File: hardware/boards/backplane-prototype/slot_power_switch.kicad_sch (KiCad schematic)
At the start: 14 parts, among them Q1 SQD50P06-15L_GE3, Q2 BSS123, U1 74HC595D,118

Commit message: chore: checkpoint current board layout
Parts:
- U1: value 74HC595D,118 -> 74HC595D
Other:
- title: Slot 1 High-Side Power Switch -> Backplane Prototype
- moved on the sheet: C1, D9, Q1, Q2, R15, R16, R17, R18, R19, R20, R21, R22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

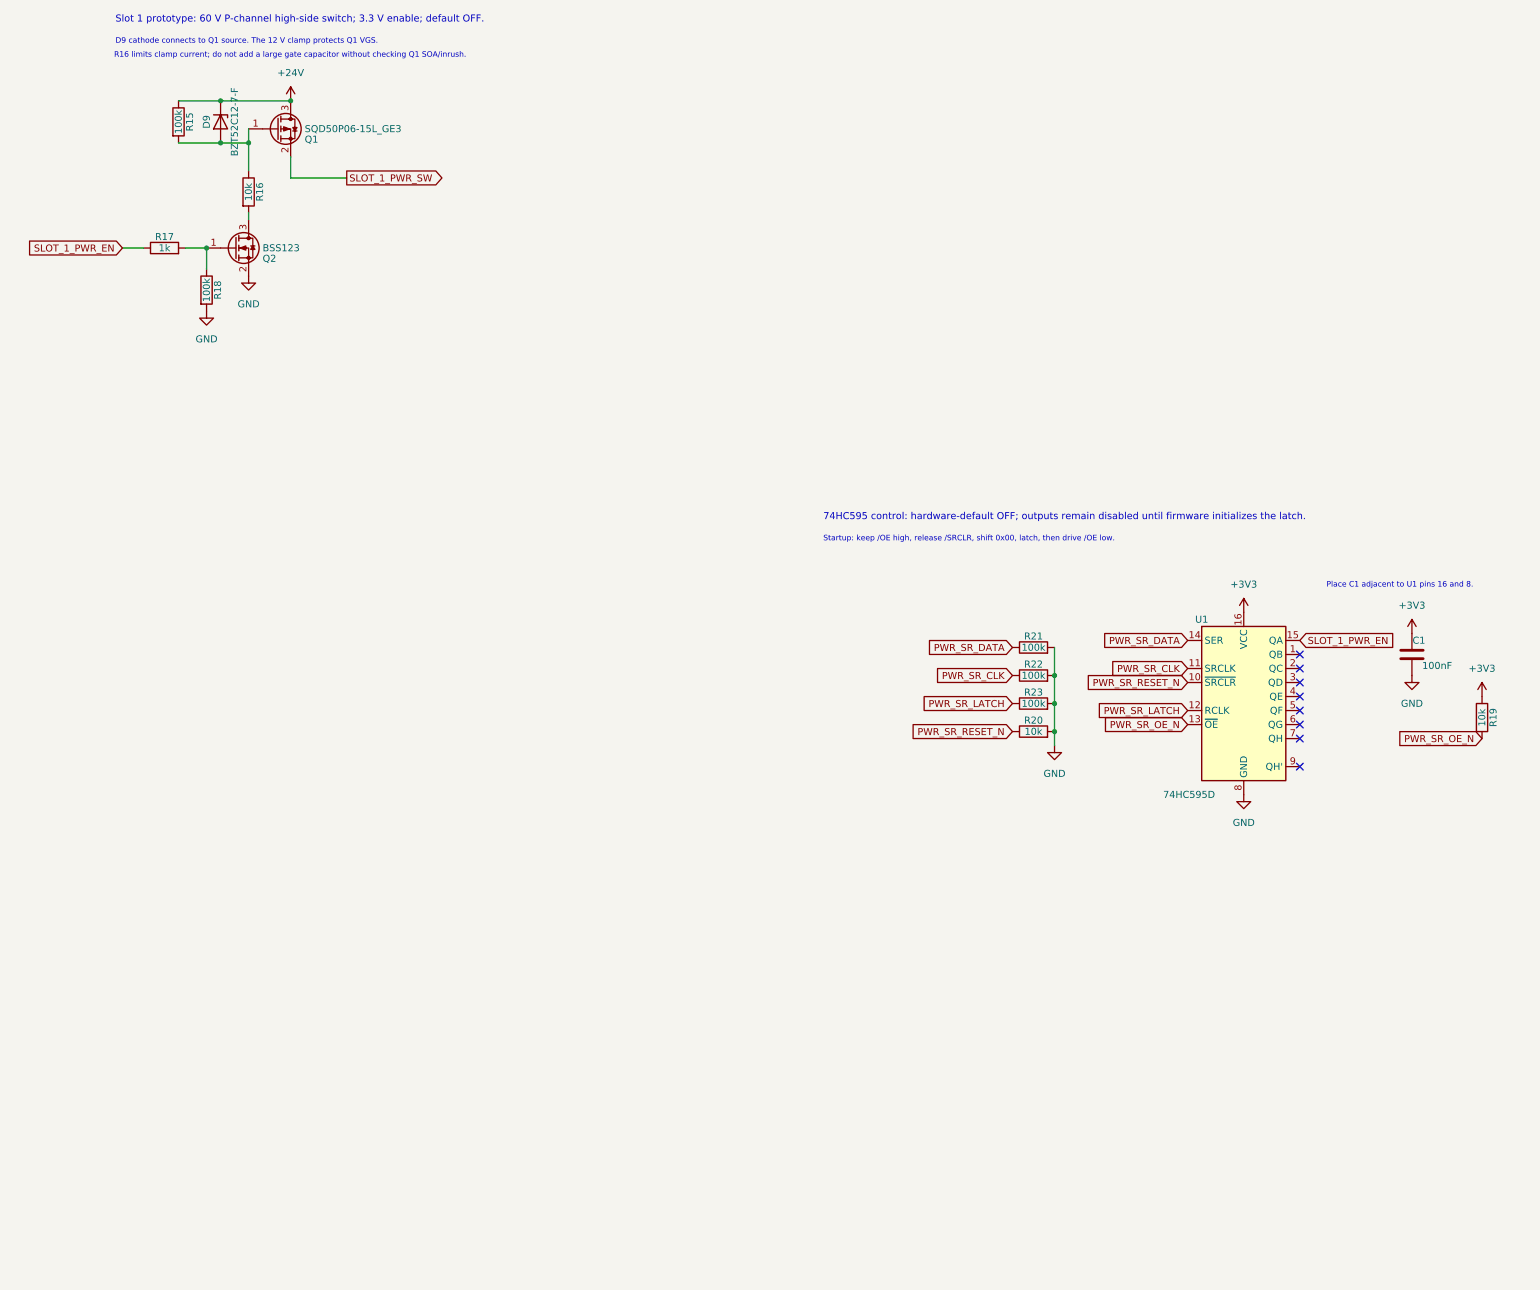
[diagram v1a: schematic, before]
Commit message: feat: add power switches for all backplane slots
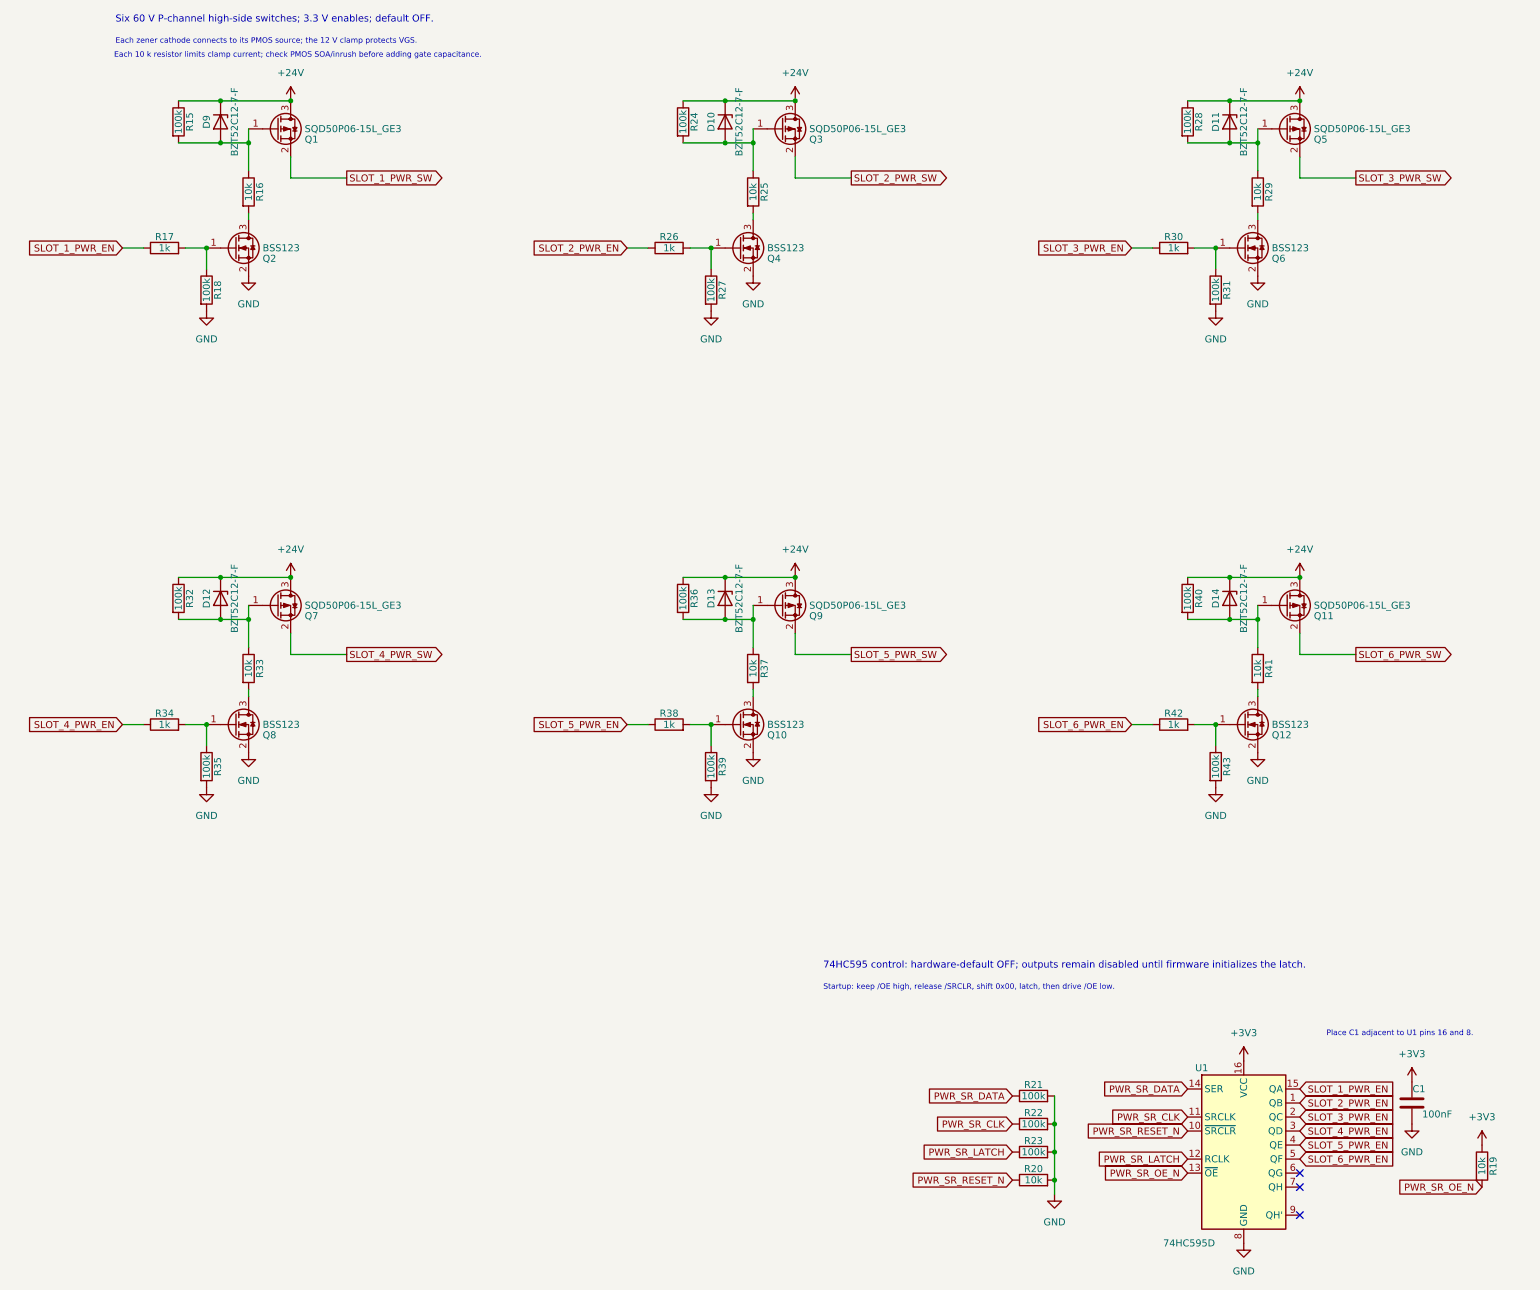
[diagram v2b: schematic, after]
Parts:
- added D10, D11, D12, D13, D14: BZT52C12-7-F, Diode_SMD:D_SOD-123, symbol Device:D_Zener
- added Q10, Q12, Q4, Q6, Q8: BSS123, Package_TO_SOT_SMD:SOT-23, symbol Transistor_FET:BSS123
- added Q11, Q3, Q5, Q7, Q9: SQD50P06-15L_GE3, Package_TO_SOT_SMD:TO-252-3_TabPin2, symbol mini-rack-power:Q_PMOS_GDS_PassiveGate
- added R24, R27, R28, R31, R32, R35, R36, R39, R40, R43: 100k, Resistor_SMD:R_0603_1608Metric, symbol Device:R
- added R25, R29, R33, R37, R41: 10k, Resistor_SMD:R_1206_3216Metric, symbol Device:R
- added R26, R30, R34, R38, R42: 1k, Resistor_SMD:R_0603_1608Metric, symbol Device:R
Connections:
- net +24V: now also D10.1 (K), D11.1 (K), D12.1 (K), D13.1 (K), D14.1 (K), Q11.3 (S), Q3.3 (S), Q5.3 (S), Q7.3 (S), Q9.3 (S), R24.1, R28.1, R32.1, R36.1, R40.1
- net GND: now also Q10.2 (S), Q12.2 (S), Q4.2 (S), Q6.2 (S), Q8.2 (S), R27.2, R31.2, R35.2, R39.2, R43.2
- net SLOT_2_PWR_EN: now reaches U1.1 (QB)
- net SLOT_2_PWR_EN: now also R26.1
- net SLOT_3_PWR_EN: now reaches U1.2 (QC)
- net SLOT_3_PWR_EN: now also R30.1
- net SLOT_4_PWR_EN: now reaches U1.3 (QD)
- net SLOT_4_PWR_EN: now also R34.1
- net SLOT_5_PWR_EN: now reaches U1.4 (QE)
- net SLOT_5_PWR_EN: now also R38.1
- net SLOT_6_PWR_EN: now reaches U1.5 (QF)
- net SLOT_6_PWR_EN: now also R42.1
- new net: D10.2 (A), Q3.1 (G), R24.2, R25.1
- new net: D12.2 (A), Q7.1 (G), R32.2, R33.1
- new net: D13.2 (A), Q9.1 (G), R36.2, R37.1
- new net: Q12.1 (G), R42.2, R43.1
- new net: Q12.3 (D), R41.2
- new net: Q10.1 (G), R38.2, R39.1
- new net: Q6.1 (G), R30.2, R31.1
- new net: D11.2 (A), Q5.1 (G), R28.2, R29.1
- new net: Q8.1 (G), R34.2, R35.1
- new net: Q4.1 (G), R26.2, R27.1
- new net: Q4.3 (D), R25.2
- new net: D14.2 (A), Q11.1 (G), R40.2, R41.1
- new net: Q10.3 (D), R37.2
- new net: Q8.3 (D), R33.2
- new net: Q6.3 (D), R29.2
- new net SLOT_2_PWR_SW: Q3.2 (D)
- new net SLOT_3_PWR_SW: Q5.2 (D)
- new net SLOT_4_PWR_SW: Q7.2 (D)
- new net SLOT_5_PWR_SW: Q9.2 (D)
- new net SLOT_6_PWR_SW: Q11.2 (D)
- no-connect marks 8 -> 3
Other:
- note added: "Each 10 k resistor limits clamp current; check PMOS SOA/inrush before adding gate capacitance."
- note added: "Each zener cathode connects to its PMOS source; the 12 V clamp protects VGS."
- note added: "Six 60 V P-channel high-side switches; 3.3 V enables; default OFF."
- note removed: "D9 cathode connects to Q1 source. The 12 V clamp protects Q1 VGS."
- note removed: "R16 limits clamp current; do not add a large gate capacitor without checking Q1 SOA/inrush."
- note removed: "Slot 1 prototype: 60 V P-channel high-side switch; 3.3 V enable; default OFF."
- moved on the sheet: C1, R19, R20, R21, R22, R23, U1

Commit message: Replace slot power shift register with PCA9554
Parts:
- removed R19, R20: 10k, Resistor_SMD:R_0603_1608Metric, symbol Device:R
- removed R21, R22, R23: 100k, Resistor_SMD:R_0603_1608Metric, symbol Device:R
- R18, R27, R31, R35, R39, R43: value 100k -> 10k; LCSC C14675 -> C25804
- U1: value 74HC595D -> PCA9554PWR; footprint Package_SO:SOIC-16_3.9x9.9mm_P1.27mm -> Package_SO:TSSOP-16_4.4x5mm_P0.65mm; symbol 74xx:74HC595 -> mini-rack-power:PCA9554PWR; LCSC C5947 -> C2873588
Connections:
- net PWR_SR_RESET_N is gone; now on net SLOT_6_PWR_EN: U1.10 (P5)
- net GND: now also U1.1 (A0), U1.2 (A1), U1.3 (A2)
- net SLOT_1_PWR_EN: now also U1.4 (P0); no longer U1.15 (QA)
- net SLOT_2_PWR_EN: now also U1.5 (P1); no longer U1.1 (QB)
- net SLOT_3_PWR_EN: now also U1.6 (P2); no longer U1.2 (QC)
- net SLOT_4_PWR_EN: now also U1.7 (P3); no longer U1.3 (QD)
- net SLOT_5_PWR_EN: now also U1.9 (P4); no longer U1.4 (QE)
- net SLOT_6_PWR_EN: no longer U1.5 (QF)
- net PWR_SR_CLK: no longer names the net of U1.11 (P6)
- net PWR_SR_DATA renamed I2C_UP_SCL
- net PWR_SR_LATCH: no longer names the net of U1.12 (P7)
- net PWR_SR_OE_N: no longer names the net of U1.13 (~{INT})
- new net I2C_UP_SDA: U1.15 (SDA)
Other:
- note added: "PCA9554 power control: A2:A0 = 000 (7-bit address 0x20); P0-P5 drive slots 1-6; P6/P7 and /INT are unused."
- note added: "Startup: 10 k gate pulldowns hold all slots OFF; write Output Port = 0x00 before configuring P0-P5 as outputs."
- note removed: "74HC595 control: hardware-default OFF; outputs remain disabled until firmware initializes the latch."
- note removed: "Startup: keep /OE high, release /SRCLR, shift 0x00, latch, then drive /OE low."
- moved on the sheet: U1

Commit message: Checkpoint: pre-autoroute
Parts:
- added C1: 100nF 100V, Capacitor_SMD:C_0603_1608Metric, symbol Device:C
- added JP1: A0_ADDR, Jumper:SolderJumper-3_P1.3mm_Bridged12_Pad1.0x1.5mm, symbol Jumper:SolderJumper_3_Bridged12
- added R13, R22, R23: 4.7k 1%, Resistor_SMD:R_0603_1608Metric, symbol Device:R
- added TP1: I2C_UP_SDA, TestPoint:TestPoint_Pad_D1.5mm, symbol Connector:TestPoint
- added TP2: I2C_UP_SCL, TestPoint:TestPoint_Pad_D1.5mm, symbol Connector:TestPoint
- added TP3, TP7: MUX_CH6_SCL, TestPoint:TestPoint_Pad_D1.5mm, symbol Connector:TestPoint
- added TP4, TP8: MUX_CH6_SDA, TestPoint:TestPoint_Pad_D1.5mm, symbol Connector:TestPoint
- added TP5: MUX_CH7_SCL, TestPoint:TestPoint_Pad_D1.5mm, symbol Connector:TestPoint
- added TP6: MUX_CH7_SDA, TestPoint:TestPoint_Pad_D1.5mm, symbol Connector:TestPoint
- added U1: TCA9548APWR, Package_SO:TSSOP-24_4.4x7.8mm_P0.65mm, symbol Interface_Expansion:TCA9548APWR
- renumbered C1 to C2, D13 to D10, D14 to D12, D9 to D7, D12 to D8, D10 to D9, Q2 to Q1, Q12 to Q10, Q5 to Q11, Q11 to Q12, Q8 to Q2, Q1 to Q3, Q7 to Q4, Q4 to Q5, Q10 to Q6, Q3 to Q7, Q9 to Q8, Q6 to Q9, R17 to R14, R34 to R15, R15 to R16, R32 to R17, R35 to R19, R16 to R20, R33 to R21, R26 to R24, R38 to R25, R24 to R26, R36 to R27, R27 to R28, R39 to R29, R25 to R30, R37 to R31, R30 to R32, R42 to R33, R28 to R34, R40 to R35, R31 to R36, R43 to R37, R29 to R38, R41 to R39, U1 to U2
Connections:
- net +3V3: now also C1.1, JP1.3 (B), R13.1, R22.1, R23.1, U1.24 (VCC)
- net GND: now also C1.2, JP1.1 (A), U1.1 (A0), U1.12 (GND), U1.2 (A1)
- net I2C_UP_SCL: now also R23.2, TP2.1, U1.22 (SCL)
- net I2C_UP_SDA: now also R22.2, TP1.1, U1.23 (SDA)
- net at U2.11 (P6): now also TP7.1
- net at U2.12 (P7): now also TP8.1
- new net: TP5.1, U1.20 (SC7)
- new net: TP3.1, U1.18 (SC6)
- new net: TP6.1, U1.19 (SD7)
- new net: JP1.2 (C), U1.21 (A2)
- new net: TP4.1, U1.17 (SD6)
- new net I2C_MUX_RESET_N: R13.2, U1.3 (~{RESET})
- new net SCL_SLOT_1: U1.5 (SC0)
- new net SCL_SLOT_2: U1.7 (SC1)
- new net SCL_SLOT_3: U1.9 (SC2)
- new net SCL_SLOT_4: U1.11 (SC3)
- new net SCL_SLOT_5: U1.14 (SC4)
- new net SCL_SLOT_6: U1.16 (SC5)
- new net SDA_SLOT_1: U1.4 (SD0)
- new net SDA_SLOT_2: U1.6 (SD1)
- new net SDA_SLOT_3: U1.8 (SD2)
- new net SDA_SLOT_4: U1.10 (SD3)
- new net SDA_SLOT_5: U1.13 (SD4)
- new net SDA_SLOT_6: U1.15 (SD5)
- no-connect marks 3 -> 1
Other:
- note added: "/RESET is pulled high by R1."
- note added: "TCA9548A U2: channels 0-5 map to slots 1-6 A2:A1:A0 = 000 (0x70)"
- note removed: "Place C1 adjacent to U1 pins 16 and 8."
- moved on the sheet: C2, U2

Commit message: Checkpoint before auto-router
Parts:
- removed JP1: A0_ADDR, Jumper:SolderJumper-3_P1.3mm_Bridged12_Pad1.0x1.5mm, symbol Jumper:SolderJumper_3_Bridged12
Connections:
- net GND: now also U1.21 (A2)

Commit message: Fix backplane connectivity and assembly metadata
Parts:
- TP1, TP2, TP3, TP4, TP5, TP6, TP7, TP8: now left out of the parts list
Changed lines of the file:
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@@
 		(body_style 1)
 		(exclude_from_sim no)
-		(in_bom yes)
+		(in_bom no)
 		(on_board yes)
 		(in_pos_files yes)
@@
 		(body_style 1)
 		(exclude_from_sim no)
-		(in_bom yes)
+		(in_bom no)
 		(on_board yes)
 		(in_pos_files yes)
@@
 		(body_style 1)
 		(exclude_from_sim no)
-		(in_bom yes)
+		(in_bom no)
 		(on_board yes)
 		(in_pos_files yes)
@@
 		(body_style 1)
 		(exclude_from_sim no)
-		(in_bom yes)
+		(in_bom no)
 		(on_board yes)
 		(in_pos_files yes)
@@
 		(body_style 1)
 		(exclude_from_sim no)
-		(in_bom yes)
+		(in_bom no)
 		(on_board yes)
 		(in_pos_files yes)
@@
 		(body_style 1)
 		(exclude_from_sim no)
-		(in_bom yes)
+		(in_bom no)
 		(on_board yes)
 		(in_pos_files yes)
@@
 		(body_style 1)
 		(exclude_from_sim no)
-		(in_bom yes)
+		(in_bom no)
 		(on_board yes)
 		(in_pos_files yes)
@@
 		(body_style 1)
 		(exclude_from_sim no)
-		(in_bom yes)
+		(in_bom no)
 		(on_board yes)
 		(in_pos_files yes)

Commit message: Remove testpoints and align remaining silkscreen
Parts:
- TP1, TP2, TP3, TP4, TP5, TP6, TP7, TP8: now not fitted
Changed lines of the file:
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@@
 		(exclude_from_sim no)
 		(in_bom no)
-		(on_board yes)
-		(in_pos_files yes)
-		(dnp no)
+		(on_board no)
+		(in_pos_files no)
+		(dnp yes)
 		(property "Reference" "TP5"
 			(at 113.03 246.126 0)
@@
 		(exclude_from_sim no)
 		(in_bom no)
-		(on_board yes)
-		(in_pos_files yes)
-		(dnp no)
+		(on_board no)
+		(in_pos_files no)
+		(dnp yes)
 		(property "Reference" "TP3"
 			(at 101.6 246.126 0)
@@
 		(exclude_from_sim no)
 		(in_bom no)
-		(on_board yes)
-		(in_pos_files yes)
-		(dnp no)
+		(on_board no)
+		(in_pos_files no)
+		(dnp yes)
 		(property "Reference" "TP6"
 			(at 118.11 246.126 0)
@@
 		(exclude_from_sim no)
 		(in_bom no)
-		(on_board yes)
-		(in_pos_files yes)
-		(dnp no)
+		(on_board no)
+		(in_pos_files no)
+		(dnp yes)
 		(property "Reference" "TP8"
 			(at 388.62 53.086 0)
@@
 		(exclude_from_sim no)
 		(in_bom no)
-		(on_board yes)
-		(in_pos_files yes)
-		(dnp no)
+		(on_board no)
+		(in_pos_files no)
+		(dnp yes)
 		(property "Reference" "TP2"
 			(at 83.312 198.12 0)
@@
 		(exclude_from_sim no)
 		(in_bom no)
-		(on_board yes)
-		(in_pos_files yes)
-		(dnp no)
+		(on_board no)
+		(in_pos_files no)
+		(dnp yes)
 		(property "Reference" "TP7"
 			(at 384.81 53.086 0)
@@
 		(exclude_from_sim no)
 		(in_bom no)
-		(on_board yes)
-		(in_pos_files yes)
-		(dnp no)
+		(on_board no)
+		(in_pos_files no)
+		(dnp yes)
 		(property "Reference" "TP1"
 			(at 56.388 198.12 0)
@@
 		(exclude_from_sim no)
 		(in_bom no)
-		(on_board yes)
-		(in_pos_files yes)
-		(dnp no)
+		(on_board no)
+		(in_pos_files no)
+		(dnp yes)
 		(property "Reference" "TP4"
 			(at 106.68 246.126 0)
